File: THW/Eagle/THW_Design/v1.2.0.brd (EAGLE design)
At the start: 100 x 200 mm, 20 parts

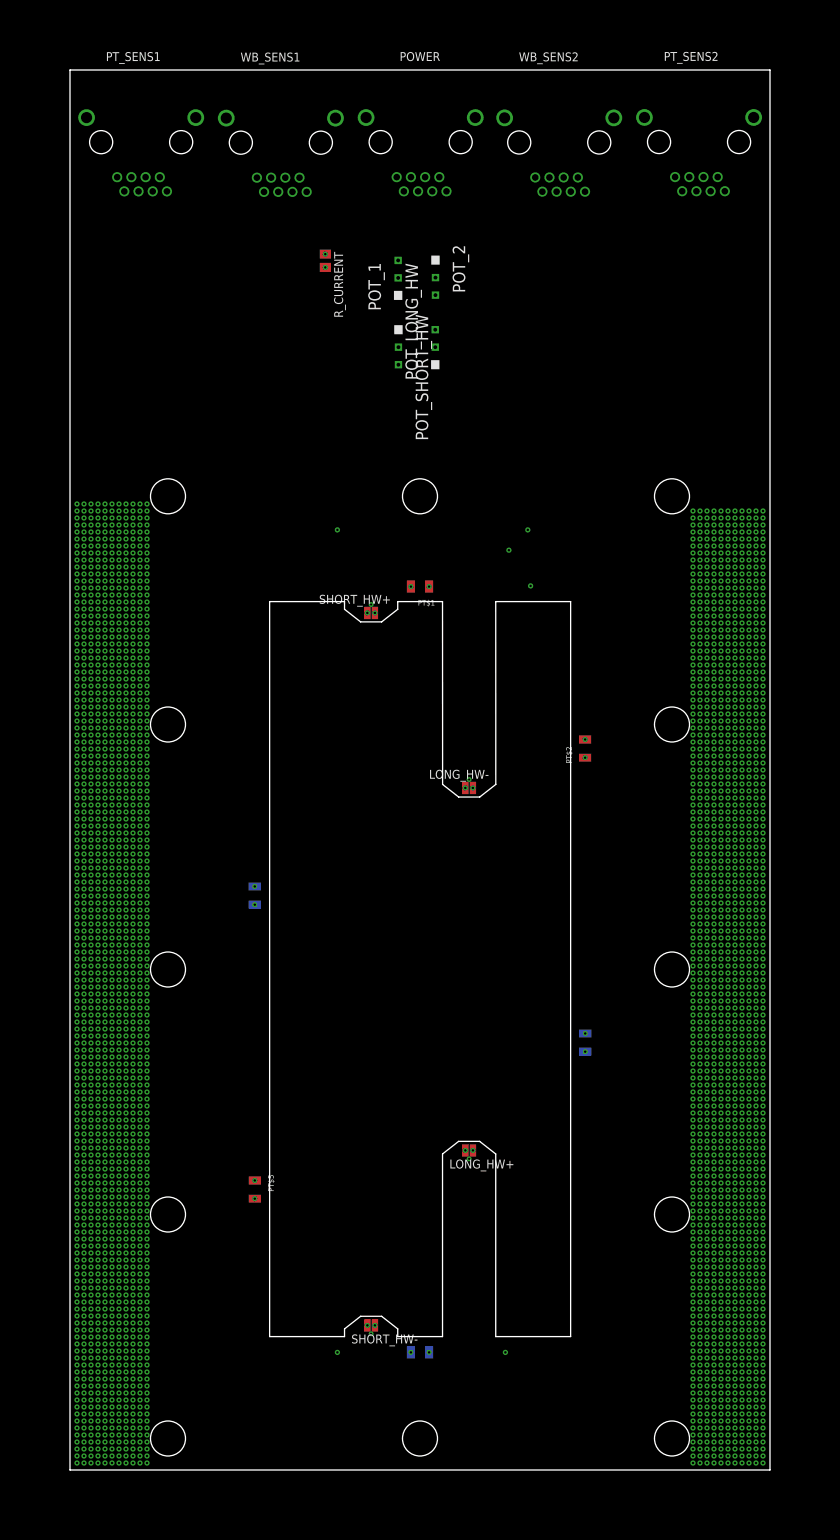
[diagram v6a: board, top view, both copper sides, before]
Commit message: peeled back solder mask for cell contacts
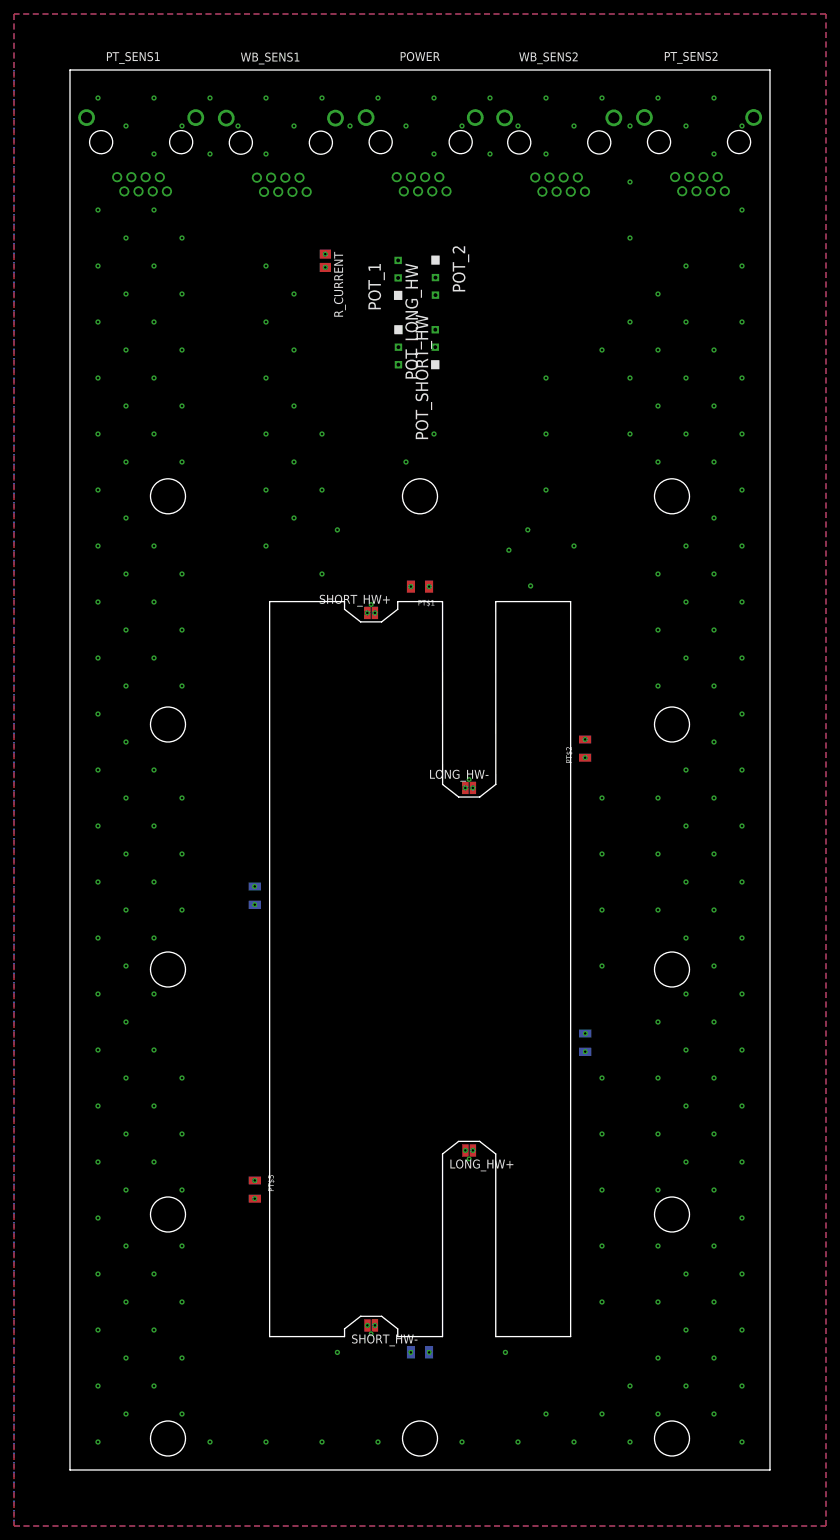
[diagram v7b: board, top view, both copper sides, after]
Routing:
- added copper zone on layer 16, net BSHEILD
- added copper zone on layer 1, net TSHEILD

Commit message: Minor changes to design and logo package
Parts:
- added U$1: (no value), AD_LOGO:AD_LOGO
